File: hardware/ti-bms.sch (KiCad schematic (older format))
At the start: 61 parts, among them J1 Conn_02x03_Odd_Even, J2 Conn_01x02, J3 Conn_01x02, J4 Conn_01x02, J5 CAN_TERM, Q1 NCV8402xST, U1 Pico, U2 MCP2515-xST, U3 SN65HVD230, U4 TPS62160DGK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

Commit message: dual wake inputs
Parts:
- removed Q1: NCV8402xST, Package_TO_SOT_SMD:SOT-223, symbol Driver_FET:NCV8402xST
- added C15: 1u, Capacitor_SMD:C_0603_1608Metric, symbol Device:C
- added D9: 3v, Diode_SMD:D_MiniMELF, symbol Device:D_Zener
- added R19: 4k7, Resistor_SMD:R_0603_1608Metric, symbol Device:R
- added R20: 1k5, Resistor_SMD:R_0603_1608Metric, symbol Device:R
- C11: value 470n -> 1u; LCSC C1623 -> C15849
- C2: LCSC C12891 -> C5672
- L1: footprint footprints:1227ASH100MP2 -> Inductor_SMD:L_Neosid_SMS-ME3015; LCSC C435389 -> C43389
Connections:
- net GND: now also C15.2, D9.2 (A), R20.2
- net IN12_1 renamed WAKE1
- net OUT1 renamed IN2
- net IN2: now also C15.1, D9.1 (K), R19.2, R20.1
- net OUT12_1 renamed WAKE2
- net WAKE2: now also R19.1
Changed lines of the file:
@@
 F 0 "L1" V 9519 1350 50  0000 C CNN
 F 1 "2.2u" V 9610 1350 50  0000 C CNN
-F 2 "footprints:1227ASH100MP2" H 9700 1350 50  0001 C CNN
+F 2 "Inductor_SMD:L_Neosid_SMS-ME3015" H 9700 1350 50  0001 C CNN
 F 3 "~" H 9700 1350 50  0001 C CNN
-F 4 "C435389" V 9700 1350 50  0001 C CNN "LCSC"
+F 4 "C43389" V 9700 1350 50  0001 C CNN "LCSC"
 	1    9700 1350
 	0    1    1    0
@@
 F 2 "Capacitor_SMD:C_1206_3216Metric" H 10438 1350 50  0001 C CNN
 F 3 "~" H 10400 1500 50  0001 C CNN
-F 4 "C12891" H 10400 1500 50  0001 C CNN "LCSC"
+F 4 "C5672" H 10400 1500 50  0001 C CNN "LCSC"
 	1    10400 1500
 	1    0    0    -1
@@
 P 1100 7100
 F 0 "C11" H 1215 7146 50  0000 L CNN
-F 1 "470n" H 1215 7055 50  0000 L CNN
+F 1 "1u" H 1215 7055 50  0000 L CNN
 F 2 "Capacitor_SMD:C_0603_1608Metric" H 1138 6950 50  0001 C CNN
 F 3 "~" H 1100 7100 50  0001 C CNN
-F 4 "C1623" H 1100 7100 50  0001 C CNN "LCSC"
+F 4 "C15849" H 1100 7100 50  0001 C CNN "LCSC"
 	1    1100 7100
 	1    0    0    -1
 $EndComp
-$Comp
-L Driver_FET:NCV8402xST Q1
-U 1 1 61DDABE2
-P 3400 6850
-F 0 "Q1" H 3828 6896 50  0000 L CNN
-F 1 "NCV8402xST" H 3828 6805 50  0000 L CNN
-F 2 "Package_TO_SOT_SMD:SOT-223" H 3400 6570 50  0001 C CNN
-F 3 "https://www.onsemi.com/pub/Collateral/NCV8402-D.PDF" H 3700 6850 50  0001 C CNN
-F 4 "C77755" H 3400 6850 50  0001 C CNN "LCSC"
-	1    3400 6850
-	1    0    0    -1
-$EndComp
-Text GLabel 2900 6850 0    50   Input ~ 0
-OUT1
-Text GLabel 3750 6400 2    50   Output ~ 0
-OUT12_1
-Wire Wire Line
-	3750 6400 3700 6400
-Wire Wire Line
-	3700 6400 3700 6450
 Wire Wire Line
 	1450 6850 1450 6950
@@
 	1    0    0    -1
 $EndComp
-$Comp
-L power:GND #PWR0109
-U 1 1 61DBD4E0
-P 3700 7250
-F 0 "#PWR0109" H 3700 7000 50  0001 C CNN
-F 1 "GND" H 3705 7077 50  0000 C CNN
-F 2 "" H 3700 7250 50  0001 C CNN
-F 3 "" H 3700 7250 50  0001 C CNN
-	1    3700 7250
-	1    0    0    -1
-$EndComp
 Text GLabel 1900 6950 2    50   Output ~ 0
 IN1
 Text GLabel 1250 6550 0    50   Input ~ 0
-IN12_1
+WAKE1
 Wire Wire Line
 	1250 6550 1450 6550
@@
 Text GLabel 7050 2300 2    50   Input ~ 0
 IN1
-Text GLabel 7050 2200 2    50   Output ~ 0
-OUT1
-Text GLabel 5550 5700 0    50   Input ~ 0
-OUT12_1
-Text GLabel 5550 5800 0    50   Output ~ 0
-IN12_1
+Text GLabel 7050 2200 2    50   Input ~ 0
+IN2
+Text GLabel 5550 5700 0    50   Output ~ 0
+WAKE2
 Text GLabel 9650 4900 0    50   Input ~ 0
 Rs
@@
 	1    0    0    -1
 $EndComp
+$Comp
+L Device:R R19
+U 1 1 61DDB629
+P 2950 6700
+F 0 "R19" H 3020 6746 50  0000 L CNN
+F 1 "4k7" H 3020 6655 50  0000 L CNN
+F 2 "Resistor_SMD:R_0603_1608Metric" V 2880 6700 50  0001 C CNN
+F 3 "~" H 2950 6700 50  0001 C CNN
+F 4 "C23162" H 2950 6700 50  0001 C CNN "LCSC"
+	1    2950 6700
+	1    0    0    -1
+$EndComp
+$Comp
+L Device:R R20
+U 1 1 61DDB7CC
+P 2950 7100
+F 0 "R20" H 3020 7146 50  0000 L CNN
+F 1 "1k5" H 3020 7055 50  0000 L CNN
+F 2 "Resistor_SMD:R_0603_1608Metric" V 2880 7100 50  0001 C CNN
+F 3 "~" H 2950 7100 50  0001 C CNN
+F 4 "C22843" H 2950 7100 50  0001 C CNN "LCSC"
+	1    2950 7100
+	1    0    0    -1
+$EndComp
+$Comp
+L Device:D_Zener D9
+U 1 1 61DDB7D7
+P 3300 7100
+F 0 "D9" V 3254 7180 50  0000 L CNN
+F 1 "3v" V 3345 7180 50  0000 L CNN
+F 2 "Diode_SMD:D_MiniMELF" H 3300 7100 50  0001 C CNN
+F 3 "~" H 3300 7100 50  0001 C CNN
+F 4 "C8056" V 3300 7100 50  0001 C CNN "LCSC"
+	1    3300 7100
+	0    1    1    0
+$EndComp
+$Comp
+L Device:C C15
+U 1 1 61DDB7E2
+P 2600 7100
+F 0 "C15" H 2715 7146 50  0000 L CNN
+F 1 "1u" H 2715 7055 50  0000 L CNN
+F 2 "Capacitor_SMD:C_0603_1608Metric" H 2638 6950 50  0001 C CNN
+F 3 "~" H 2600 7100 50  0001 C CNN
+F 4 "C15849" H 2600 7100 50  0001 C CNN "LCSC"
+	1    2600 7100
+	1    0    0    -1
+$EndComp
+Wire Wire Line
+	2950 6850 2950 6950
+Wire Wire Line
+	2600 6950 2950 6950
+Connection ~ 2950 6950
+Wire Wire Line
+	2600 7250 2950 7250
+Wire Wire Line
+	2950 7250 3300 7250
+Connection ~ 2950 7250
+Wire Wire Line
+	3300 6950 2950 6950
+$Comp
+L power:GND #PWR0109
+U 1 1 61DDB7F3
+P 2950 7250
+F 0 "#PWR0109" H 2950 7000 50  0001 C CNN
+F 1 "GND" H 2955 7077 50  0000 C CNN
+F 2 "" H 2950 7250 50  0001 C CNN
+F 3 "" H 2950 7250 50  0001 C CNN
+	1    2950 7250
+	1    0    0    -1
+$EndComp
+Text GLabel 3400 6950 2    50   Output ~ 0
+IN2
+Text GLabel 2750 6550 0    50   Input ~ 0
+WAKE2
+Wire Wire Line
+	2750 6550 2950 6550
+Wire Wire Line
+	3300 6950 3400 6950
+Connection ~ 3300 6950
+Text GLabel 5550 5800 0    50   Output ~ 0
+WAKE1
 $EndSCHEMATC

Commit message: rework inputs
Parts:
- C11, C15: value 1u -> 100n; LCSC C15849 -> C14663
- D6, D9: value 3v -> 3.3v
- R13, R19: value 4k7 -> 47k; LCSC C23162 -> C25819
- R14, R20: value 1k5 -> 4.7k; LCSC C22843 -> C23162
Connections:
- net GND: now also R13.2, R19.2; no longer R14.2, R20.2
- net IN1: now also R14.2; no longer R13.2, R14.1
- net IN2: now also R20.2; no longer R19.2, R20.1
- net WAKE1: now also R14.1
- net WAKE2: now also R20.1
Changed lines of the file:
@@
 	8450 3250 8450 3350
-$Comp
-L Device:R R13
-U 1 1 61DD7F66
-P 1450 6700
-F 0 "R13" H 1520 6746 50  0000 L CNN
-F 1 "4k7" H 1520 6655 50  0000 L CNN
-F 2 "Resistor_SMD:R_0603_1608Metric" V 1380 6700 50  0001 C CNN
-F 3 "~" H 1450 6700 50  0001 C CNN
-F 4 "C23162" H 1450 6700 50  0001 C CNN "LCSC"
-	1    1450 6700
-	1    0    0    -1
-$EndComp
-$Comp
-L Device:R R14
-U 1 1 61DD8D2C
-P 1450 7100
-F 0 "R14" H 1520 7146 50  0000 L CNN
-F 1 "1k5" H 1520 7055 50  0000 L CNN
-F 2 "Resistor_SMD:R_0603_1608Metric" V 1380 7100 50  0001 C CNN
-F 3 "~" H 1450 7100 50  0001 C CNN
-F 4 "C22843" H 1450 7100 50  0001 C CNN "LCSC"
-	1    1450 7100
-	1    0    0    -1
-$EndComp
-$Comp
-L Device:D_Zener D6
-U 1 1 61DD9637
-P 1800 7100
-F 0 "D6" V 1754 7180 50  0000 L CNN
-F 1 "3v" V 1845 7180 50  0000 L CNN
-F 2 "Diode_SMD:D_MiniMELF" H 1800 7100 50  0001 C CNN
-F 3 "~" H 1800 7100 50  0001 C CNN
-F 4 "C8056" V 1800 7100 50  0001 C CNN "LCSC"
-	1    1800 7100
-	0    1    1    0
-$EndComp
-$Comp
-L Device:C C11
-U 1 1 61DD9B38
-P 1100 7100
-F 0 "C11" H 1215 7146 50  0000 L CNN
-F 1 "1u" H 1215 7055 50  0000 L CNN
-F 2 "Capacitor_SMD:C_0603_1608Metric" H 1138 6950 50  0001 C CNN
-F 3 "~" H 1100 7100 50  0001 C CNN
-F 4 "C15849" H 1100 7100 50  0001 C CNN "LCSC"
-	1    1100 7100
-	1    0    0    -1
-$EndComp
-Wire Wire Line
-	1450 6850 1450 6950
-Wire Wire Line
-	1100 6950 1450 6950
-Connection ~ 1450 6950
-Wire Wire Line
-	1100 7250 1450 7250
-Wire Wire Line
-	1450 7250 1800 7250
-Connection ~ 1450 7250
-Wire Wire Line
-	1800 6950 1450 6950
 $Comp
 L power:GND #PWR0108
 U 1 1 61DBD09A
-P 1450 7250
-F 0 "#PWR0108" H 1450 7000 50  0001 C CNN
-F 1 "GND" H 1455 7077 50  0000 C CNN
-F 2 "" H 1450 7250 50  0001 C CNN
-F 3 "" H 1450 7250 50  0001 C CNN
-	1    1450 7250
-	1    0    0    -1
-$EndComp
-Text GLabel 1900 6950 2    50   Output ~ 0
-IN1
-Text GLabel 1250 6550 0    50   Input ~ 0
+P 1850 7050
+F 0 "#PWR0108" H 1850 6800 50  0001 C CNN
+F 1 "GND" H 1855 6877 50  0000 C CNN
+F 2 "" H 1850 7050 50  0001 C CNN
+F 3 "" H 1850 7050 50  0001 C CNN
+	1    1850 7050
+	1    0    0    -1
+$EndComp
+Text GLabel 1500 6450 0    50   Input ~ 0
 WAKE1
-Wire Wire Line
-	1250 6550 1450 6550
-Wire Wire Line
-	1800 6950 1900 6950
-Connection ~ 1800 6950
 Text GLabel 7050 2300 2    50   Input ~ 0
 IN1
@@
 	1    0    0    -1
 $EndComp
-$Comp
-L Device:R R19
-U 1 1 61DDB629
-P 2950 6700
-F 0 "R19" H 3020 6746 50  0000 L CNN
-F 1 "4k7" H 3020 6655 50  0000 L CNN
-F 2 "Resistor_SMD:R_0603_1608Metric" V 2880 6700 50  0001 C CNN
-F 3 "~" H 2950 6700 50  0001 C CNN
-F 4 "C23162" H 2950 6700 50  0001 C CNN "LCSC"
-	1    2950 6700
-	1    0    0    -1
-$EndComp
-$Comp
-L Device:R R20
-U 1 1 61DDB7CC
-P 2950 7100
-F 0 "R20" H 3020 7146 50  0000 L CNN
-F 1 "1k5" H 3020 7055 50  0000 L CNN
-F 2 "Resistor_SMD:R_0603_1608Metric" V 2880 7100 50  0001 C CNN
-F 3 "~" H 2950 7100 50  0001 C CNN
-F 4 "C22843" H 2950 7100 50  0001 C CNN "LCSC"
-	1    2950 7100
-	1    0    0    -1
-$EndComp
-$Comp
-L Device:D_Zener D9
-U 1 1 61DDB7D7
-P 3300 7100
-F 0 "D9" V 3254 7180 50  0000 L CNN
-F 1 "3v" V 3345 7180 50  0000 L CNN
-F 2 "Diode_SMD:D_MiniMELF" H 3300 7100 50  0001 C CNN
-F 3 "~" H 3300 7100 50  0001 C CNN
-F 4 "C8056" V 3300 7100 50  0001 C CNN "LCSC"
-	1    3300 7100
-	0    1    1    0
-$EndComp
-$Comp
-L Device:C C15
-U 1 1 61DDB7E2
-P 2600 7100
-F 0 "C15" H 2715 7146 50  0000 L CNN
-F 1 "1u" H 2715 7055 50  0000 L CNN
-F 2 "Capacitor_SMD:C_0603_1608Metric" H 2638 6950 50  0001 C CNN
-F 3 "~" H 2600 7100 50  0001 C CNN
-F 4 "C15849" H 2600 7100 50  0001 C CNN "LCSC"
-	1    2600 7100
-	1    0    0    -1
-$EndComp
-Wire Wire Line
-	2950 6850 2950 6950
-Wire Wire Line
-	2600 6950 2950 6950
-Connection ~ 2950 6950
-Wire Wire Line
-	2600 7250 2950 7250
-Wire Wire Line
-	2950 7250 3300 7250
-Connection ~ 2950 7250
-Wire Wire Line
-	3300 6950 2950 6950
-$Comp
-L power:GND #PWR0109
-U 1 1 61DDB7F3
-P 2950 7250
-F 0 "#PWR0109" H 2950 7000 50  0001 C CNN
-F 1 "GND" H 2955 7077 50  0000 C CNN
-F 2 "" H 2950 7250 50  0001 C CNN
-F 3 "" H 2950 7250 50  0001 C CNN
-	1    2950 7250
-	1    0    0    -1
-$EndComp
-Text GLabel 3400 6950 2    50   Output ~ 0
-IN2
-Text GLabel 2750 6550 0    50   Input ~ 0
-WAKE2
-Wire Wire Line
-	2750 6550 2950 6550
-Wire Wire Line
-	3300 6950 3400 6950
-Connection ~ 3300 6950
 Text GLabel 5550 5800 0    50   Output ~ 0
 WAKE1
+Text GLabel 2300 6750 2    50   Output ~ 0
+IN1
+$Comp
+L Device:R R14
+U 1 1 61DFFFFD
+P 1850 6600
+F 0 "R14" H 1920 6646 50  0000 L CNN
+F 1 "4.7k" H 1920 6555 50  0000 L CNN
+F 2 "Resistor_SMD:R_0603_1608Metric" V 1780 6600 50  0001 C CNN
+F 3 "~" H 1850 6600 50  0001 C CNN
+F 4 "C23162" H 1850 6600 50  0001 C CNN "LCSC"
+	1    1850 6600
+	1    0    0    -1
+$EndComp
+$Comp
+L Device:D_Zener D6
+U 1 1 61E008E3
+P 1850 6900
+F 0 "D6" V 1804 6980 50  0000 L CNN
+F 1 "3.3v" V 1895 6980 50  0000 L CNN
+F 2 "Diode_SMD:D_MiniMELF" H 1850 6900 50  0001 C CNN
+F 3 "~" H 1850 6900 50  0001 C CNN
+F 4 "C8056" V 1850 6900 50  0001 C CNN "LCSC"
+	1    1850 6900
+	0    1    1    0
+$EndComp
+$Comp
+L Device:C C11
+U 1 1 61E0357F
+P 2200 6900
+F 0 "C11" H 2315 6946 50  0000 L CNN
+F 1 "100n" H 2315 6855 50  0000 L CNN
+F 2 "Capacitor_SMD:C_0603_1608Metric" H 2238 6750 50  0001 C CNN
+F 3 "~" H 2200 6900 50  0001 C CNN
+F 4 "C14663" H 2200 6900 50  0001 C CNN "LCSC"
+	1    2200 6900
+	1    0    0    -1
+$EndComp
+$Comp
+L Device:R R13
+U 1 1 61E0A2F4
+P 1550 6750
+F 0 "R13" H 1620 6796 50  0000 L CNN
+F 1 "47k" H 1620 6705 50  0000 L CNN
+F 2 "Resistor_SMD:R_0603_1608Metric" V 1480 6750 50  0001 C CNN
+F 3 "~" H 1550 6750 50  0001 C CNN
+F 4 "C25819" H 1550 6750 50  0001 C CNN "LCSC"
+	1    1550 6750
+	1    0    0    -1
+$EndComp
+Wire Wire Line
+	1850 7050 1550 7050
+Wire Wire Line
+	1550 7050 1550 6900
+Connection ~ 1850 7050
+Wire Wire Line
+	1850 6450 1550 6450
+Wire Wire Line
+	1550 6450 1550 6600
+Wire Wire Line
+	1500 6450 1550 6450
+Connection ~ 1550 6450
+Wire Wire Line
+	2200 6750 1850 6750
+Connection ~ 1850 6750
+Wire Wire Line
+	1850 7050 2200 7050
+Wire Wire Line
+	2300 6750 2200 6750
+Connection ~ 2200 6750
+$Comp
+L power:GND #PWR0109
+U 1 1 61E3B8D0
+P 3350 7050
+F 0 "#PWR0109" H 3350 6800 50  0001 C CNN
+F 1 "GND" H 3355 6877 50  0000 C CNN
+F 2 "" H 3350 7050 50  0001 C CNN
+F 3 "" H 3350 7050 50  0001 C CNN
+	1    3350 7050
+	1    0    0    -1
+$EndComp
+Text GLabel 3000 6450 0    50   Input ~ 0
+WAKE2
+Text GLabel 3800 6750 2    50   Output ~ 0
+IN2
+$Comp
+L Device:R R20
+U 1 1 61E3B923
+P 3350 6600
+F 0 "R20" H 3420 6646 50  0000 L CNN
+F 1 "4.7k" H 3420 6555 50  0000 L CNN
+F 2 "Resistor_SMD:R_0603_1608Metric" V 3280 6600 50  0001 C CNN
+F 3 "~" H 3350 6600 50  0001 C CNN
+F 4 "C23162" H 3350 6600 50  0001 C CNN "LCSC"
+	1    3350 6600
+	1    0    0    -1
+$EndComp
+$Comp
+L Device:D_Zener D9
+U 1 1 61E3B92E
+P 3350 6900
+F 0 "D9" V 3304 6980 50  0000 L CNN
+F 1 "3.3v" V 3395 6980 50  0000 L CNN
+F 2 "Diode_SMD:D_MiniMELF" H 3350 6900 50  0001 C CNN
+F 3 "~" H 3350 6900 50  0001 C CNN
+F 4 "C8056" V 3350 6900 50  0001 C CNN "LCSC"
+	1    3350 6900
+	0    1    1    0
+$EndComp
+$Comp
+L Device:C C15
+U 1 1 61E3B939
+P 3700 6900
+F 0 "C15" H 3815 6946 50  0000 L CNN
+F 1 "100n" H 3815 6855 50  0000 L CNN
+F 2 "Capacitor_SMD:C_0603_1608Metric" H 3738 6750 50  0001 C CNN
+F 3 "~" H 3700 6900 50  0001 C CNN
+F 4 "C14663" H 3700 6900 50  0001 C CNN "LCSC"
+	1    3700 6900
+	1    0    0    -1
+$EndComp
+$Comp
+L Device:R R19
+U 1 1 61E3B944
+P 3050 6750
+F 0 "R19" H 3120 6796 50  0000 L CNN
+F 1 "47k" H 3120 6705 50  0000 L CNN
+F 2 "Resistor_SMD:R_0603_1608Metric" V 2980 6750 50  0001 C CNN
+F 3 "~" H 3050 6750 50  0001 C CNN
+F 4 "C25819" H 3050 6750 50  0001 C CNN "LCSC"
+	1    3050 6750
+	1    0    0    -1
+$EndComp
+Wire Wire Line
+	3350 7050 3050 7050
+Wire Wire Line
+	3050 7050 3050 6900
+Connection ~ 3350 7050
+Wire Wire Line
+	3350 6450 3050 6450
+Wire Wire Line
+	3050 6450 3050 6600
+Wire Wire Line
+	3000 6450 3050 6450
+Connection ~ 3050 6450
+Wire Wire Line
+	3700 6750 3350 6750
+Connection ~ 3350 6750
+Wire Wire Line
+	3350 7050 3700 7050
+Wire Wire Line
+	3800 6750 3700 6750
+Connection ~ 3700 6750
 $EndSCHEMATC

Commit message: finish inputs
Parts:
- R14, R20: value 4.7k -> 5.6k; LCSC C23162 -> C23189
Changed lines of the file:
@@
 P 1850 6600
 F 0 "R14" H 1920 6646 50  0000 L CNN
-F 1 "4.7k" H 1920 6555 50  0000 L CNN
+F 1 "5.6k" H 1920 6555 50  0000 L CNN
 F 2 "Resistor_SMD:R_0603_1608Metric" V 1780 6600 50  0001 C CNN
 F 3 "~" H 1850 6600 50  0001 C CNN
-F 4 "C23162" H 1850 6600 50  0001 C CNN "LCSC"
+F 4 "C23189" H 1850 6600 50  0001 C CNN "LCSC"
 	1    1850 6600
 	1    0    0    -1
@@
 P 3350 6600
 F 0 "R20" H 3420 6646 50  0000 L CNN
-F 1 "4.7k" H 3420 6555 50  0000 L CNN
+F 1 "5.6k" H 3420 6555 50  0000 L CNN
 F 2 "Resistor_SMD:R_0603_1608Metric" V 3280 6600 50  0001 C CNN
 F 3 "~" H 3350 6600 50  0001 C CNN
-F 4 "C23162" H 3350 6600 50  0001 C CNN "LCSC"
+F 4 "C23189" H 3350 6600 50  0001 C CNN "LCSC"
 	1    3350 6600
 	1    0    0    -1

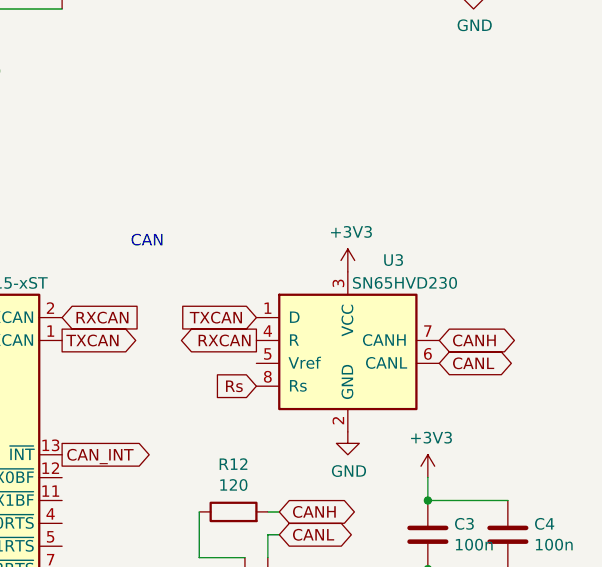
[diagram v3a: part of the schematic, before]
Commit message: swap in available part
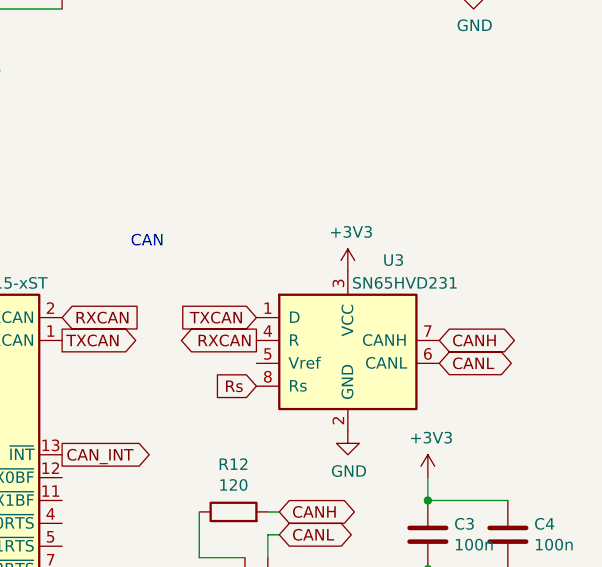
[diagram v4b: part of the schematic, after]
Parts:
- U3: value SN65HVD230 -> SN65HVD231; LCSC C12084 -> C129257
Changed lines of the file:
@@
 P 10050 4700
 F 0 "U3" H 10250 5050 50  0000 C CNN
-F 1 "SN65HVD230" H 10300 4950 50  0000 C CNN
+F 1 "SN65HVD231" H 10300 4950 50  0000 C CNN
 F 2 "Package_SO:SOIC-8_3.9x4.9mm_P1.27mm" H 10050 4200 50  0001 C CNN
 F 3 "http://www.ti.com/lit/ds/symlink/sn65hvd230.pdf" H 9950 5100 50  0001 C CNN
-F 4 "C12084" H 10050 4700 50  0001 C CNN "LCSC"
+F 4 "C129257" H 10050 4700 50  0001 C CNN "LCSC"
 	1    10050 4700
 	1    0    0    -1

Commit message: merge v3 improvements into v2
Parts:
- removed C11, C14, C15: 100n, Capacitor_SMD:C_0603_1608Metric, symbol Device:C
- removed C12, C13: 1n 1000v, Capacitor_SMD:C_1206_3216Metric, symbol Device:C
- removed D6, D9: 3.3v, Diode_SMD:D_MiniMELF, symbol Device:D_Zener
- removed D7, D8: 5v, footprints:SOD882, symbol Device:D_Zener
- removed J2, J3, J4: Conn_01x02, Connector_Molex:Molex_Micro-Fit_3.0_43650-0200_1x02_P3.00mm_Horizontal, symbol Connector_Generic:Conn_01x02
- removed L4: 22u, footprints:ACT45B-101-2P-TL003, symbol Device:L_Core_Ferrite_Coupled_1324
- removed R13, R19: 47k, Resistor_SMD:R_0603_1608Metric, symbol Device:R
- removed R14, R20: 5.6k, Resistor_SMD:R_0603_1608Metric, symbol Device:R
- removed R15, R16: 1k, Resistor_SMD:R_0603_1608Metric, symbol Device:R
- removed R17, R18: 10, Resistor_SMD:R_0603_1608Metric, symbol Device:R
- removed U7: MAX3485, Package_SO:SOP-8_3.9x4.9mm_P1.27mm, symbol Interface_UART:MAX3485
- added J1: Conn_02x04_Odd_Even, Connector_Molex:Molex_Micro-Fit_3.0_43045-0800_2x04_P3.00mm_Horizontal, symbol Connector_Generic:Conn_02x04_Top_Bottom
- C2: LCSC C5672 -> C12891
- L1: footprint Inductor_SMD:L_Neosid_SMS-ME3015 -> footprints:1227ASH100MP2; LCSC C43389 -> C435389
- U3: value SN65HVD231 -> SN65HVD230; LCSC C129257 -> C12084
- renumbered J1 to J2, J5 to J4
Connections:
- net RXD_3 is gone; now on net RXD_2: U1.17 (GPIO13)
- net RXE_3 is gone; now on net RXE_2: U1.16 (GPIO12)
- net TXD_3 is gone; now on net TXD_2: U1.14 (GPIO10)
- net TXE_3 is gone; now on net TXE_2: U1.15 (GPIO11)
- net B1+: now also C5.1, J1.8 (Pin_8); no longer C6.1
- net B1-: now also C6.1, J1.4 (Pin_4); no longer C5.1
- net B2+: now also C7.1, J1.1 (Pin_1); no longer C8.1
- net B2-: now also C8.1, J1.5 (Pin_5); no longer C7.1
- net GND: now also U3.8 (Rs)
- net RXD_2: no longer U1.12 (GPIO9)
- net RXE_2: no longer U1.11 (GPIO8)
- net TXD_2: no longer U1.9 (GPIO6)
- net TXE_2: no longer U1.10 (GPIO7)
- net at L2.3: now also C5.2; no longer C6.2
- net at L2.4: now also C6.2; no longer C5.2
- net at L3.3: now also C7.2; no longer C8.2
- net at L3.4: now also C8.2; no longer C7.2
- net IN1: no longer names the net of U1.31 (GPIO26_ADC0)
- net IN2: no longer names the net of U1.32 (GPIO27_ADC1)
- net Rs: no longer names the net of U1.29 (GPIO22)
- net Rs: no longer U3.8 (Rs)
- net WAKE1 renamed EVSE_PP
- net WAKE2 renamed EVSE_CP
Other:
- note added: "5-15v power supply"
- moved on the sheet: C1, C10, C2, C5, C6, C7, C8, C9, D1, D2, D3, D4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
